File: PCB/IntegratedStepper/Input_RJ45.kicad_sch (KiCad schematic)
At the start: 8 parts, among them CN1 PJ-35825, CN2 PJ-35825, J5 Conn_01x05_Socket, U4 XT30PW-F, U5 XT30PW-F

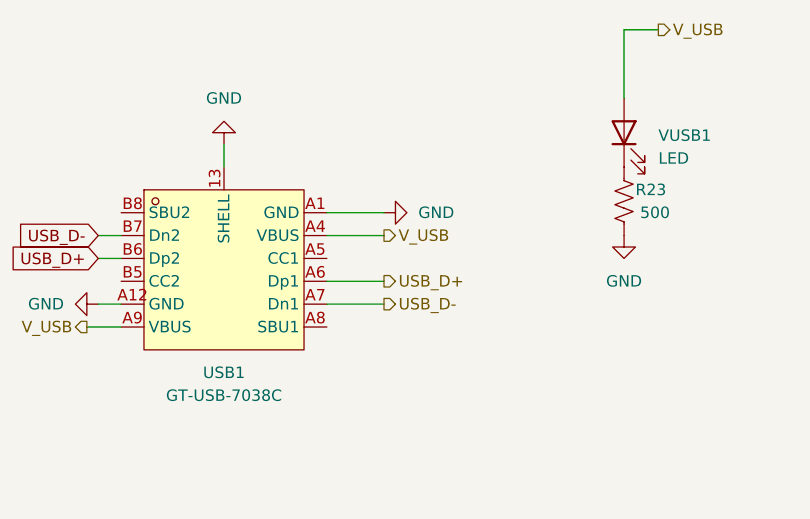
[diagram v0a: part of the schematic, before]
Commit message: update layout with pinout changes
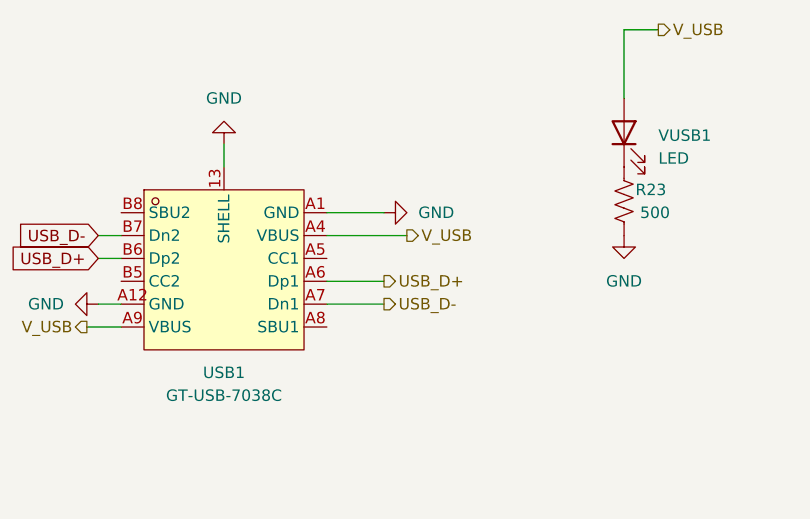
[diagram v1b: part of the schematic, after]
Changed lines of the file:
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@@
 	(wire
 		(pts
-			(xy 64.77 53.34) (xy 71.12 53.34)
+			(xy 64.77 53.34) (xy 73.66 53.34)
 		)
 		(stroke
@@
 	(hierarchical_label "V_USB"
 		(shape output)
-		(at 71.12 53.34 0)
+		(at 73.66 53.34 0)
 		(fields_autoplaced yes)
 		(effects
@@
 		)
 		(property "Intersheetrefs" "${INTERSHEET_REFS}"
-			(at 79.2089 53.34 0)
+			(at 81.7489 53.34 0)
 			(effects
 				(font

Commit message: Update final layout, replace CAN w/ JST
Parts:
- removed CN1, CN2: PJ-35825, easyeda2kicad:AUDIO-SMD_PJ-35825, symbol easyeda2kicad:PJ-35825
- added U6, U7: SM04B-GHS-TB(LF)(SN), easyeda2kicad:CONN-SMD_4P-P1.25_SM04B-GHS-TB-LF-SN, symbol easyeda2kicad:SM04B-GHS-TB(LF)(SN)
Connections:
- net CANH: now also U6.2, U7.2
- net CANL: now also U6.3, U7.3
- net GND: now also U6.4, U6.5, U6.6, U7.4, U7.5, U7.6
